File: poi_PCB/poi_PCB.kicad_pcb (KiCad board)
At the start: 2 copper layers, 60 x 60 mm, 41 parts, among them J4 USB_C_Receptacle_USB2.0, Q3 Q_NMOS_DGS, SW1 SW_Push, U1 ESP32-WROOM-32D, U2 CH340C, U3 AMS1117-3.3, U6 MH-CD42

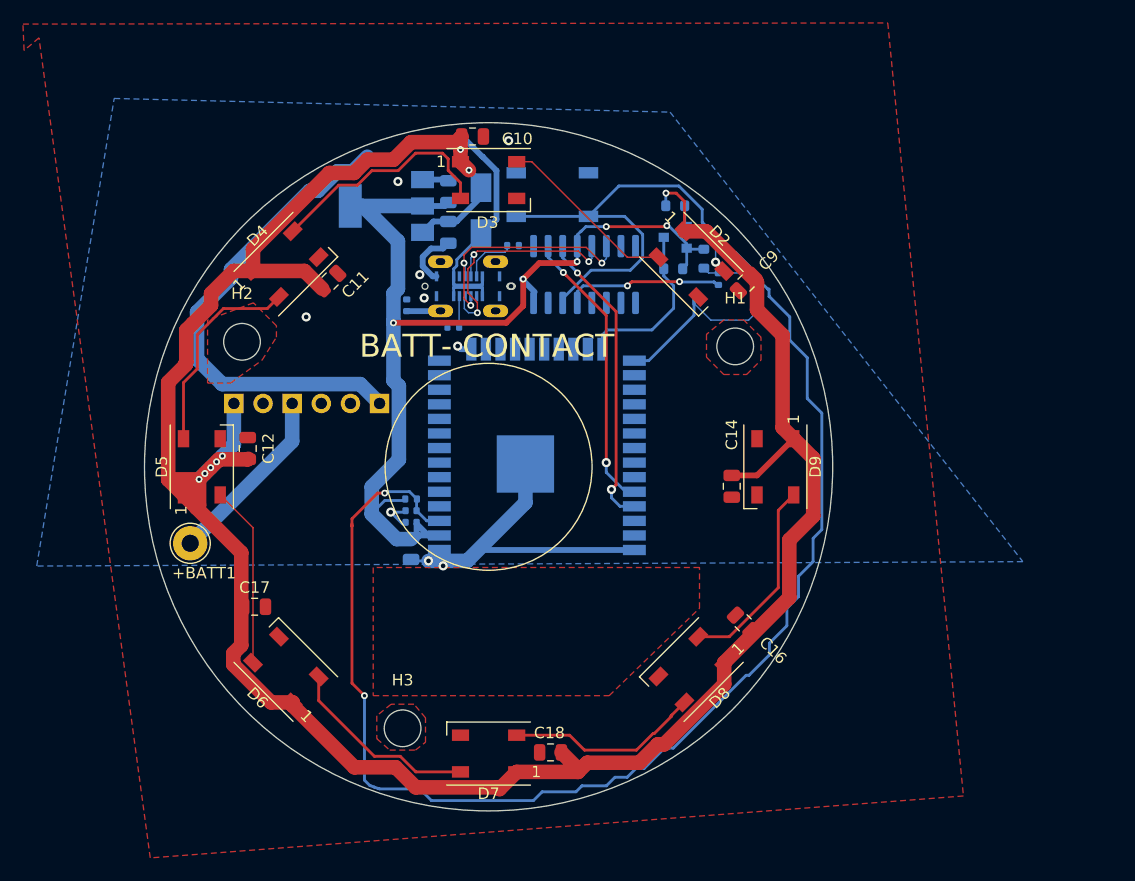
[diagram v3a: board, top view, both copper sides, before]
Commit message: redone traces, changed accelerometer, supercapacitor and mic
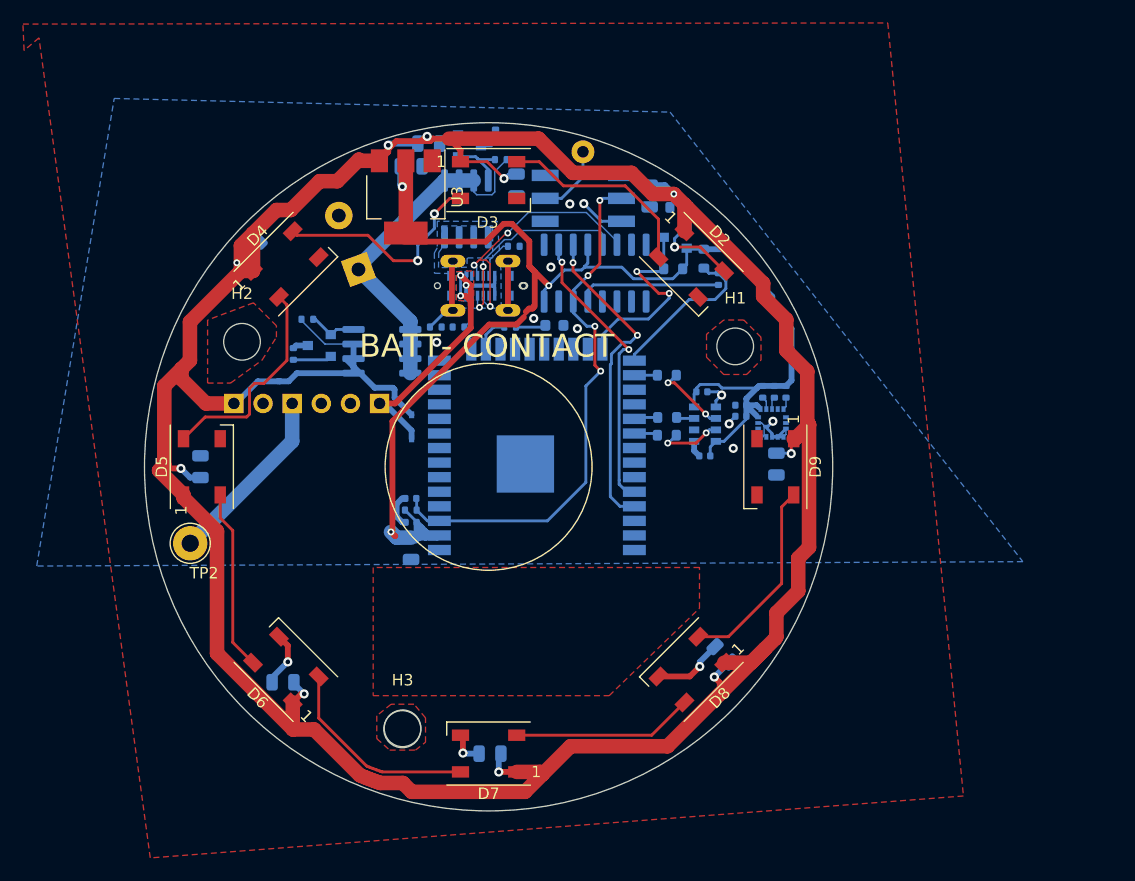
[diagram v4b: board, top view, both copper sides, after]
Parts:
- removed SW1: SW_Push, Button_Switch_SMD:SW_SPST_TL3342
- added C13: .1uF, Capacitor_SMD:C_0402_1005Metric, B.Cu at (129.5, 72.1)
- added C15: .1uF, Capacitor_SMD:C_0402_1005Metric, B.Cu at (129.5, 73.1)
- added C2: .1uF, Capacitor_SMD:C_0402_1005Metric, B.Cu at (126.3, 76.5)
- added C3: 220pF, Capacitor_SMD:C_0402_1005Metric, B.Cu at (126.1, 71.0)
- added C4: CP1_Small, Capacitor_THT:CP_Radial_D13.0mm_P5.00mm, B.Cu at (96.2, 60.3)
- added D1: LED, LED_SMD:LED_0603_1608Metric, B.Cu at (113.2, 65.2)
- added MK1: CMM-4030D-261-I2S-TR, CMM-4030D-261-I2S-TR:MIC_CMM-4030D-261-I2S-TR, B.Cu at (126.4, 73.8)
- added Q1: AO4407C, Package_SO:SOIC-8_3.9x4.9mm_P1.27mm, B.Cu at (98.2, 67.4)
- added Q2: AO3400A, Package_TO_SOT_SMD:SOT-23, B.Cu at (92.7, 66.9)
- added Q4: AO3400A, Package_TO_SOT_SMD:SOT-23, B.Cu at (105.8, 49.5)
- added Q5: AO4407C, Package_SO:SOIC-8_3.9x4.9mm_P1.27mm, B.Cu at (105.6, 55.0)
- added R11: 10K, Resistor_SMD:R_0402_1005Metric, B.Cu at (91.7, 64.6)
- added R13: 10K, Resistor_SMD:R_0402_1005Metric, B.Cu at (90.5, 67.7)
- added R17: 10K, Resistor_SMD:R_0402_1005Metric, B.Cu at (108.1, 48.6)
- added R18: 10K, Resistor_SMD:R_0402_1005Metric, B.Cu at (108.6, 50.7)
- added R19: 10K, Resistor_SMD:R_0402_1005Metric, B.Cu at (132.4, 71.0)
- added R20: 10K, Resistor_SMD:R_0402_1005Metric, B.Cu at (131.4, 71.0)
- added R21: 10K, Resistor_SMD:R_0402_1005Metric, B.Cu at (133.4, 71.0)
- added R5: 220R, Resistor_SMD:R_0402_1005Metric, B.Cu at (109.4, 65.3)
- added R7: 51R, Resistor_SMD:R_0603_1608Metric, B.Cu at (123.1, 73.2)
- added R8: 51R, Resistor_SMD:R_0603_1608Metric, B.Cu at (123.0, 69.5)
- added R9: 51R, Resistor_SMD:R_0603_1608Metric, B.Cu at (123.0, 74.7)
- added SW: TL2233OA, TL2233OA:TL2233OA, B.Cu at (115.8, 54.1)
- added TP1: 5V_EN_L, TestPoint:TestPoint_Keystone_5000-5004_Miniature, B.Cu at (115.7, 50.0)
- added U4: LSM6DS33TR, LSM6DS33TR:PQFN50P300X300X86-16N, B.Cu at (132.2, 73.7)
- C10, C11, C12, C14, C16, C17, C18, C9: moved to B.Cu
- D10: value D_Schottky_Small -> 1N5819WS; footprint Diode_SMD:D_SMA -> Diode_SMD:D_SOD-323
- Q3: value Q_NMOS_DGS -> AO3400A
- TP2: renamed from +BATT1; value TestPoint -> +BAT
- U3: moved to F.Cu
- moved D10 19.8 mm to (100.8, 74.0)
- moved C9 11.3 mm to (121.5, 53.9), turned to 270 degrees
- moved C7 7.92 mm to (102.3, 49.3), turned to 0 degrees
- moved C11 7.41 mm to (86.8, 58.5)
- moved C17 7.04 mm to (89.6, 96.3), turned to 180 degrees
- moved C10 5.71 mm to (109.9, 52.9), turned to 270 degrees
- moved C18 5.28 mm to (107.6, 102.5)
- moved C12 4.42 mm to (82.4, 77.5)
- moved C14 4.35 mm to (132.6, 77.3)
- moved C8 3.92 mm to (100.8, 51.3), turned to 0 degrees
- moved C16 3.27 mm to (127.9, 93.8)
- moved R1 3.17 mm to (102.9, 65.3), turned to 180 degrees
- moved U3 1.87 mm to (100.3, 54.0), turned to 270 degrees
- moved J4 1.08 mm to (106.8, 61.7)
- moved C1 1.07 mm to (100.7, 80.3)
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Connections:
- J4 pad S1: Net-(J4-PadS1) -> /SHIELD
- J4 pad S2: (no net) -> /SHIELD
- J4 pad S3: (no net) -> /SHIELD
- J4 pad S4: (no net) -> /SHIELD
- R1 pad 1: Net-(J4-PadS1) -> GND
- R1 pad 2: GND -> /SHIELD
- U1 pad 16: (no net) -> Net-(R5-Pad2)
- U1 pad 26: (no net) -> /BCLK
- U1 pad 29: (no net) -> /WS
- U1 pad 30: (no net) -> /D_OUT_I2S
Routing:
- net /RST: track 155.4 -> 47.0 mm, vias 2 -> 4
- net +5V: track 221.1 -> 277.4 mm, vias 8 -> 10
- net /VBUS: track 76.9 -> 35.7 mm, vias 0 -> 3
- net +3V3: track 93.2 -> 127.6 mm, vias 5 -> 3
- net Net-(C4-Pad1): track 0.00 -> 30.6 mm
- net /SHIELD: track 0.00 -> 11.3 mm
- net /GPIO0: track 23.9 -> 14.0 mm
- net /5V_EN_L: track 0.00 -> 6.64 mm
- net Net-(MK1-Pad6): track 0.00 -> 6.46 mm, vias 0 -> 2
- net Net-(Q4-Pad1): track 0.00 -> 5.94 mm
- net Net-(MK1-Pad7): track 0.00 -> 5.71 mm, vias 0 -> 2
- net GND: track 45.1 -> 40.8 mm, vias 9 -> 13
- net Net-(Q1-Pad4): track 0.00 -> 4.26 mm
- net /FIRE: track 0.00 -> 3.53 mm
- net /D+: track 22.1 -> 18.7 mm, vias 3 -> 2
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- added copper zone on B.Cu, net /SHIELD
- added copper zone on B.Cu, net /VBUS
- added copper zone on F.Cu, net /VBUS
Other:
- outline, holes or cut-outs redrawn
- net class Default: clearance 0.2 -> 0.2032; trace_width 0.25 -> 0.127
- rule trace_clearance: 0.2 -> 0.2032

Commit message: Verified pinouts
-Pinouts all checked to be compatible with peripherals.
-FIRE is pulled up to +CAP, and drains within 20 minutes if the device is turned off
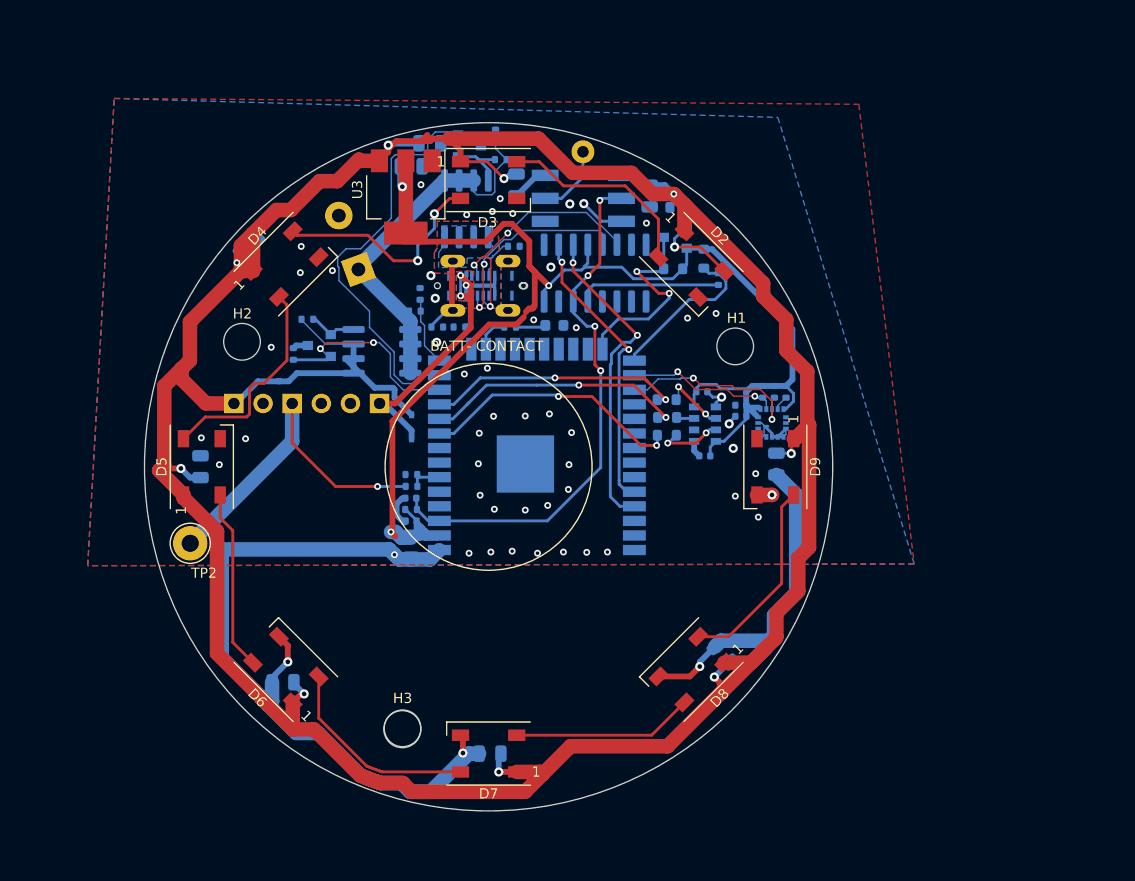
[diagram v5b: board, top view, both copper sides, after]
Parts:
- added R12: 10K, Resistor_SMD:R_0402_1005Metric, B.Cu at (133.4, 71.0)
- added R16: 100K, Resistor_SMD:R_0402_1005Metric, B.Cu at (100.8, 79.2)
- added R22: 100K, Resistor_SMD:R_0402_1005Metric, B.Cu at (101.1, 63.9)
- added R23: 100K, Resistor_SMD:R_0402_1005Metric, B.Cu at (101.5, 62.4)
- R1: value 10K -> 1K
- R21: value 10K -> 100K
- TP1: footprint TestPoint:TestPoint_Keystone_5000-5004_Miniature -> TestPoint:TestPoint_Loop_D1.80mm_Drill1.0mm_Beaded
- moved R21 33.5 mm to (100.8, 78.2), turned to 180 degrees
- moved R8 2.13 mm to (123.0, 71.6)
- moved C11 0.40 mm to (86.6, 58.1)
- moved C5 0.20 mm to (100.7, 84.4)
- moved R1 0.13 mm to (103.0, 65.3)
- moved C6 0.13 mm to (100.7, 82.2)
- moved C7 0.10 mm to (102.4, 49.3)
- moved R3 0.08 mm to (105.0, 65.3)
- moved R10 0.06 mm to (100.7, 81.2)
- turned R17 to 270 degrees
- renumbered SW to SW3
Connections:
- J4 pad S3: /SHIELD -> (no net)
- J4 pad S4: /SHIELD -> (no net)
- Q4 pad 2: /FIRE -> /FIRE_L
- R17 pad 1: GND -> /FIRE_L
- R17 pad 2: /FIRE -> Net-(C4-Pad1)
- R21 pad 1: +3V3 -> /BAT_VSENSE
- R21 pad 2: /CS -> GND
- U1 pad 10: (no net) -> /WS
- U1 pad 11: (no net) -> /BCLK
- U1 pad 12: (no net) -> /CHARGE_CAP_EN
- U1 pad 13: (no net) -> /FIRE_L
- U1 pad 14: (no net) -> /CAP_VSENSE
- U1 pad 26: /BCLK -> /SCL
- U1 pad 27: (no net) -> /SDA
- U1 pad 29: /WS -> (no net)
- U1 pad 30: /D_OUT_I2S -> (no net)
- U1 pad 6: (no net) -> /BAT_VSENSE
- U1 pad 9: (no net) -> /D_OUT_I2S
- U4 pad 4: (no net) -> /SDO
- U4 pad 5: /CS -> +3V3
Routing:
- net GND: track 40.8 -> 124.0 mm, vias 13 -> 55
- net /FIRE_L: track 0.00 -> 39.2 mm
- net /WS: track 2.08 -> 23.1 mm, vias 0 -> 2
- net /D_OUT_I2S: track 2.07 -> 23.1 mm, vias 0 -> 2
- net /BCLK: track 2.01 -> 22.4 mm, vias 0 -> 2
- net /SDA: track 1.08 -> 16.9 mm, vias 0 -> 2
- net +BATT: track 15.9 -> 30.8 mm, vias 0 -> 1
- net /CHARGE_CAP_EN: track 3.38 -> 18.0 mm, vias 0 -> 2
- net /SCL: track 1.13 -> 13.6 mm, vias 0 -> 2
- net /CAP_VSENSE: track 0.00 -> 6.01 mm
- net /SHIELD: track 11.3 -> 6.97 mm
- net /FIRE: track 3.53 -> 0.00 mm
- net /BAT_VSENSE: track 0.00 -> 3.06 mm
- net Net-(C4-Pad1): track 30.6 -> 32.6 mm
- net +3V3: track 127.6 -> 129.5 mm
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
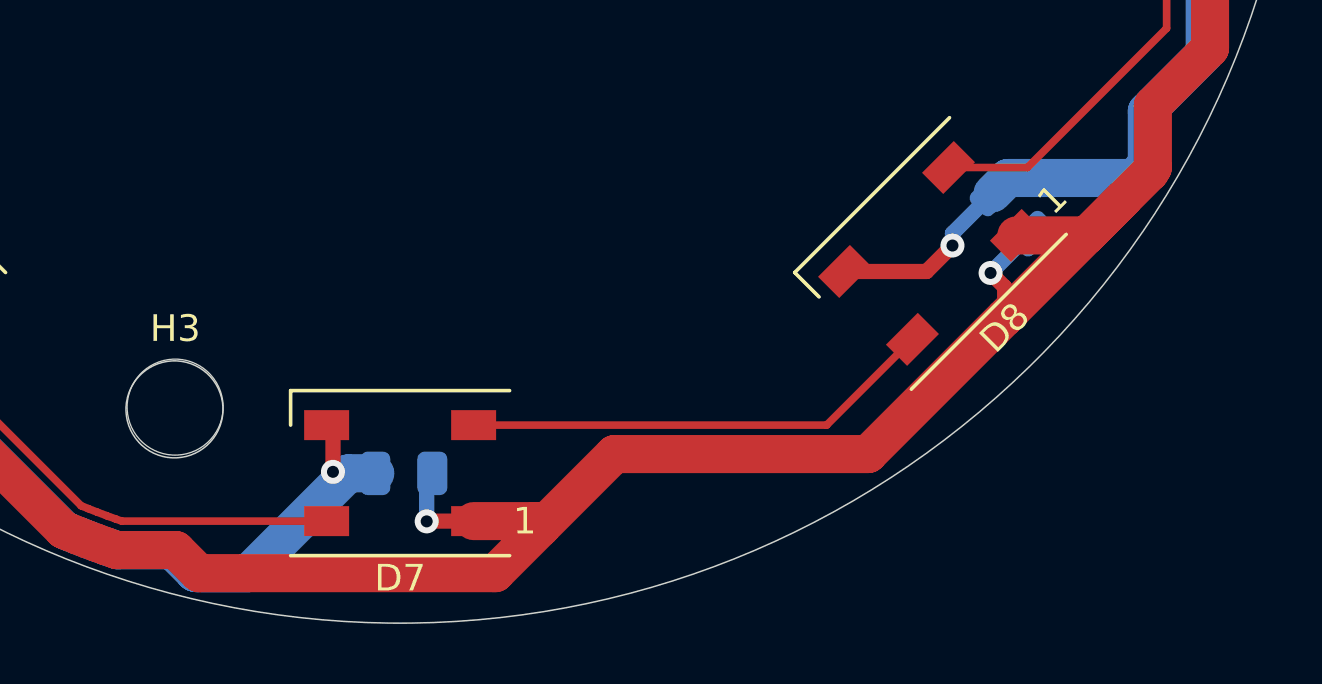
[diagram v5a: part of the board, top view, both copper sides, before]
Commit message: updated sourcing info
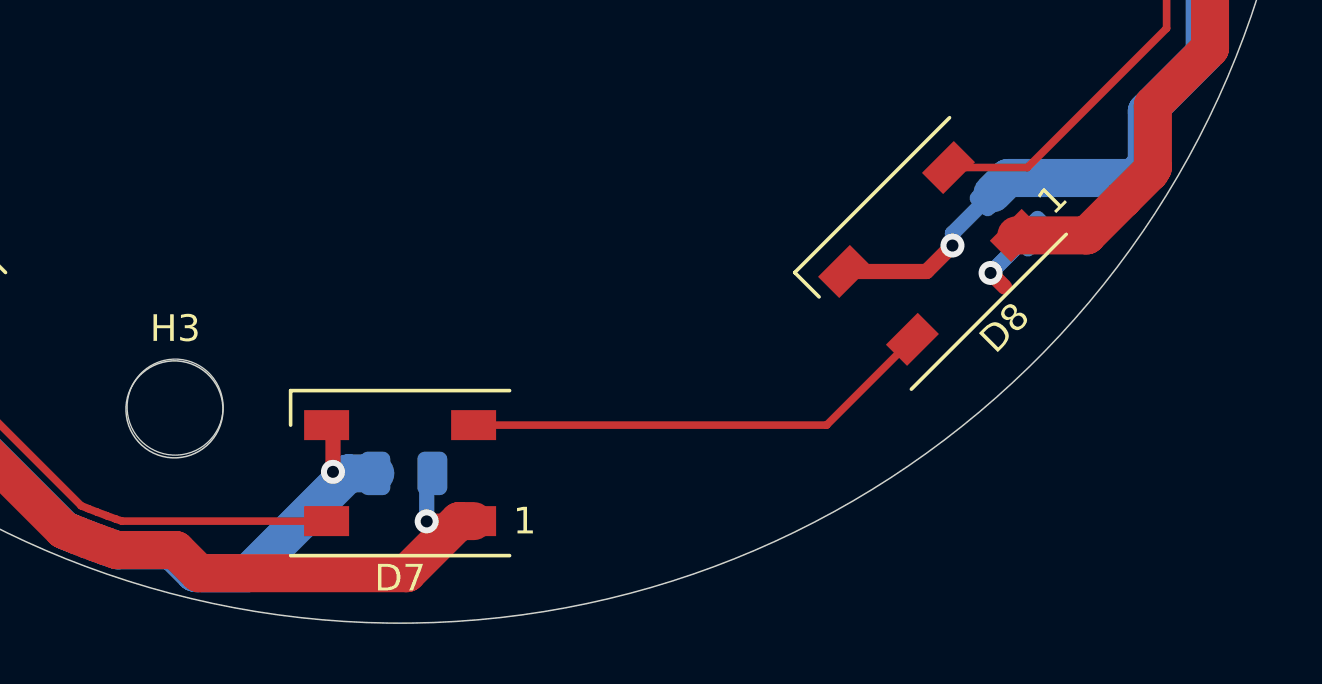
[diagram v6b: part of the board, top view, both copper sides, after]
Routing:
- net +5V: track 276.4 -> 247.0 mm

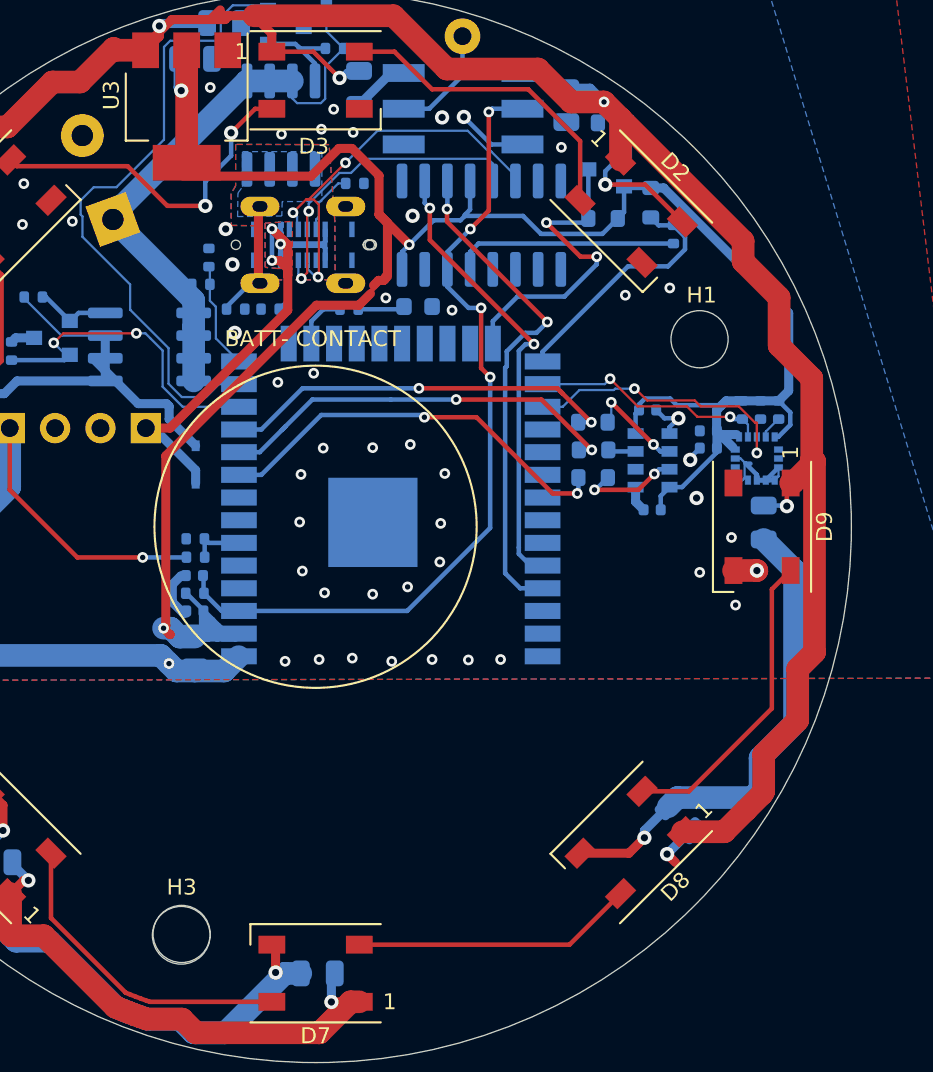
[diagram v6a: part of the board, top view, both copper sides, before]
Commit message: Updated pictures and schematics, added analog RGB header
analog RGB header is designed for 12V analog RGB strips
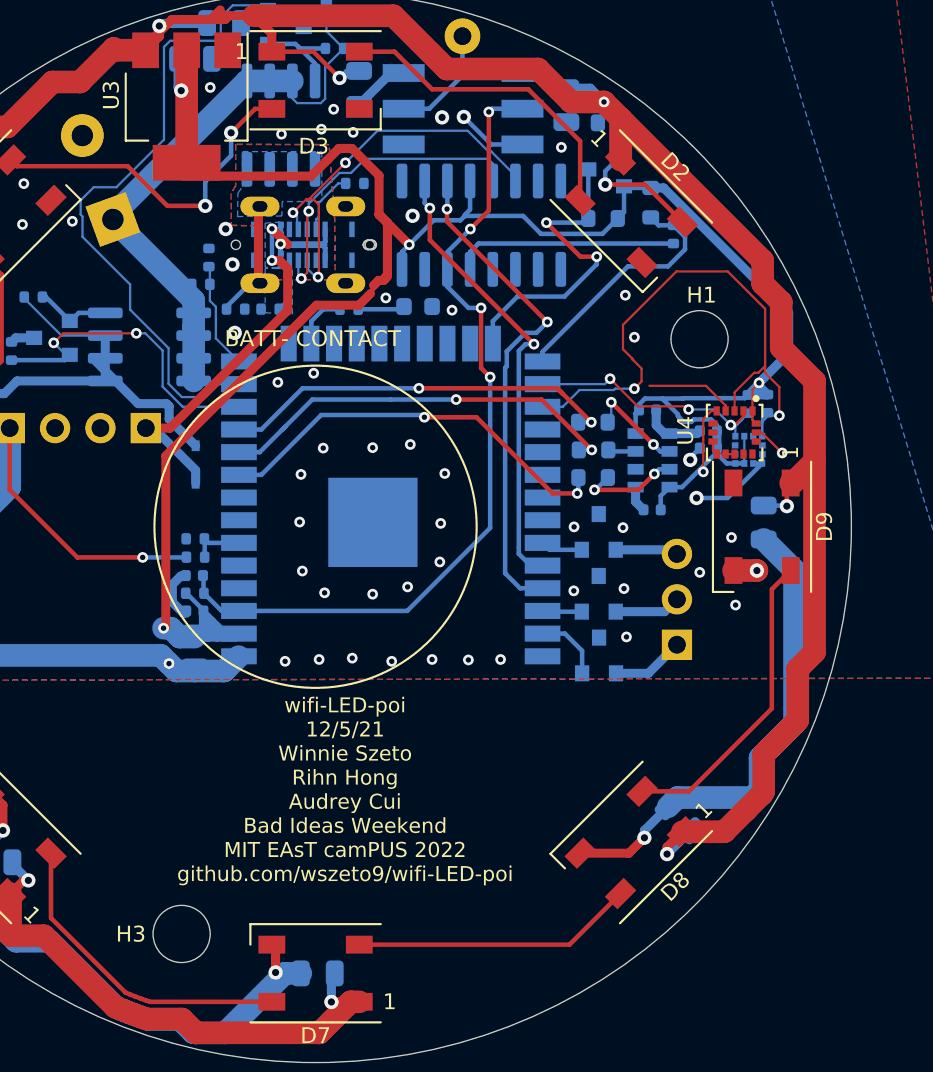
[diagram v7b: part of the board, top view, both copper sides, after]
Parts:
- removed R12: 10K, Resistor_SMD:R_0402_1005Metric
- added J1: ANALOG_RGB_HEADER, Connector_PinHeader_2.54mm:PinHeader_1x03_P2.54mm_Vertical, B.Cu at (127.7, 84.1)
- added Q6: AO3400A, Package_TO_SOT_SMD:SOT-23, B.Cu at (123.4, 77.8)
- added Q7: AO3400A, Package_TO_SOT_SMD:SOT-23, B.Cu at (123.4, 81.3)
- added Q8: AO3400A, Package_TO_SOT_SMD:SOT-23, B.Cu at (123.4, 84.7)
- added U5: LIS2DH, Package_LGA:LGA-12_2x2mm_P0.5mm, B.Cu at (131.8, 73.2)
- C1: value 1uF -> 100nF
- U4: moved to F.Cu
- moved U4 1.92 mm to (131.0, 72.2)
- moved R19 0.53 mm to (132.8, 70.6)
- moved R20 0.47 mm to (131.7, 70.6)
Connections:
- U1 pad 33: (no net) -> /RED
- U1 pad 36: (no net) -> /GREEN
- U1 pad 37: (no net) -> /BLUE
- U4 pad 4: /SDO -> GND
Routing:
- net /SDA: track 16.9 -> 32.9 mm
- net GND: track 124.0 -> 132.6 mm, vias 55 -> 60
- net +3V3: track 129.5 -> 138.0 mm, vias 3 -> 5
- net Net-(J1-Pad3): track 0.00 -> 4.12 mm
- net Net-(J1-Pad1): track 0.00 -> 4.07 mm
- net /BLUE: track 0.00 -> 3.87 mm
- net Net-(J1-Pad2): track 0.00 -> 3.71 mm
- net /RED: track 0.00 -> 2.36 mm
- net /GREEN: track 0.00 -> 2.21 mm
- net /SCL: track 13.6 -> 15.6 mm, vias 2 -> 3
- net /VBUS: track 35.7 -> 34.0 mm
- net /SDO: track 1.31 -> 0.00 mm
- net +5V: track 247.0 -> 247.9 mm
- removed copper zone on F.Cu, net /VBUS
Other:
- outline, holes or cut-outs redrawn
- board text added: "wifi-LED-poi 12/5/21 Winnie Szeto Rihn Hong Audrey Cui Bad Ideas Weekend MIT EAsT camPUS 2022 github.com/wszeto9/wifi-LED-poi"
